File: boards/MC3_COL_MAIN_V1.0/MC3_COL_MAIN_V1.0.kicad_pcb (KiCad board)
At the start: 4 copper layers, 66 x 66 mm, 121 parts, among them J1 SUPPLY_IN, J10 MOTOR, J11 MOTOR, J12 CAN, J2 SWD, J3 ENC_leaf1, J4 ENC_leaf2, J5 ENC_leaf3, J6 ENC_leaf4, J7 MOTOR, J8 MOTOR, J9 MOTOR, Q1 AO4407C, SW1 SKRKAEE020, U1 AMS1117-3.3, U10 GP1S094HCZ0F, U11 GP1S094HCZ0F, U2 STM32F412RET6, U3 DRV8214RTER, U4 DRV8214RTER, U5 DRV8214RTER, U6 DRV8214RTER, U7 DRV8214RTER, U8 TJA1051T/3, U9 AEDR-8300-1Q0, Y1 8MHz

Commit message: WIP checkpoint before LED chain (board session state as on disk)
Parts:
- added C38: 1nF, MC3_COL_MAIN:C_0402_1005Metric, F.Cu at (85.8, 94.8)
- added C39: 1nF, MC3_COL_MAIN:C_0402_1005Metric, B.Cu at (81.0, 96.8)
- added C40: 1nF, MC3_COL_MAIN:C_0402_1005Metric, B.Cu at (76.0, 93.3)
- added C41: 1nF, MC3_COL_MAIN:C_0402_1005Metric, B.Cu at (79.2, 92.8)
- added C42: 1nF, MC3_COL_MAIN:C_0402_1005Metric, F.Cu at (86.2, 93.0)
- added C43: 100nF, MC3_COL_MAIN:C_0402_1005Metric, F.Cu at (108.0, 116.0)
- added H1: M2, MC3_COL_MAIN:MountingHole_2.2mm_M2, F.Cu at (89.5, 76.0)
- added H2: M2, MC3_COL_MAIN:MountingHole_2.2mm_M2, B.Cu at (125.5, 115.5)
- added H3: M2, MC3_COL_MAIN:MountingHole_2.2mm_M2, F.Cu at (100.0, 128.0)
- added H4: M2, MC3_COL_MAIN:MountingHole_2.2mm_M2, F.Cu at (125.0, 85.0)
- added H5: SLOT-PASSTHRU, MC3_COL_MAIN:SlotNPTH_PassThrough, F.Cu at (100.4, 73.8)
- U2: value STM32F412RET6 -> STM32U595RJT6
- moved J12 30.9 mm to (127.7, 102.0)
- moved R36 9.83 mm to (101.2, 117.0)
- moved U10 8.96 mm to (97.7, 119.1), turned to 83.23 degrees
- moved U11 8.57 mm to (102.3, 80.9), turned to 83.23 degrees
- moved TP7 8.06 mm to (129.8, 106.5)
- moved R37 7.17 mm to (100.8, 122.0)
- moved TP3 6.44 mm to (118.9, 114.0)
- moved C37 5.91 mm to (124.8, 107.0), turned to 180 degrees
- moved R33 2.57 mm to (120.3, 111.0), turned to 0 degrees
- moved TP2 2.35 mm to (127.2, 104.2)
- moved C6 2.12 mm to (84.2, 87.0), turned to 90 degrees
- moved C5 1.84 mm to (85.8, 97.8)
- moved TP1 1.68 mm to (115.1, 115.2)
- moved R35 1.57 mm to (122.2, 112.1)
- moved J11 0.64 mm to (97.5, 84.6)
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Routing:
- net /CAN/CANL: track 16.4 -> 49.7 mm
- net /CAN/CANH: track 27.8 -> 59.8 mm
- net /MCU/YAW_LIM: track 17.6 -> 34.4 mm, vias 0 -> 1
- net ENC_leaf2: track 38.3 -> 47.7 mm
- net +3V3: track 225.5 -> 231.6 mm
- net I2C1_SDA: track 94.6 -> 100.1 mm
- net I2C1_SCL: track 96.5 -> 102.0 mm
- net EN_leaf1: track 42.8 -> 47.4 mm
- net Net-(U11-A): track 4.84 -> 9.34 mm
- net /MCU/YAW_HOME: track 21.0 -> 24.7 mm, vias 0 -> 1
- net RC_OUT_leaf1: track 44.4 -> 48.0 mm
- net IPROPI_leaf3: track 47.3 -> 50.8 mm
- net PH_leaf1: track 42.8 -> 45.5 mm
- net IPROPI_leaf2: track 44.7 -> 47.4 mm
- net nFAULT_leaf1: track 38.4 -> 41.0 mm
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
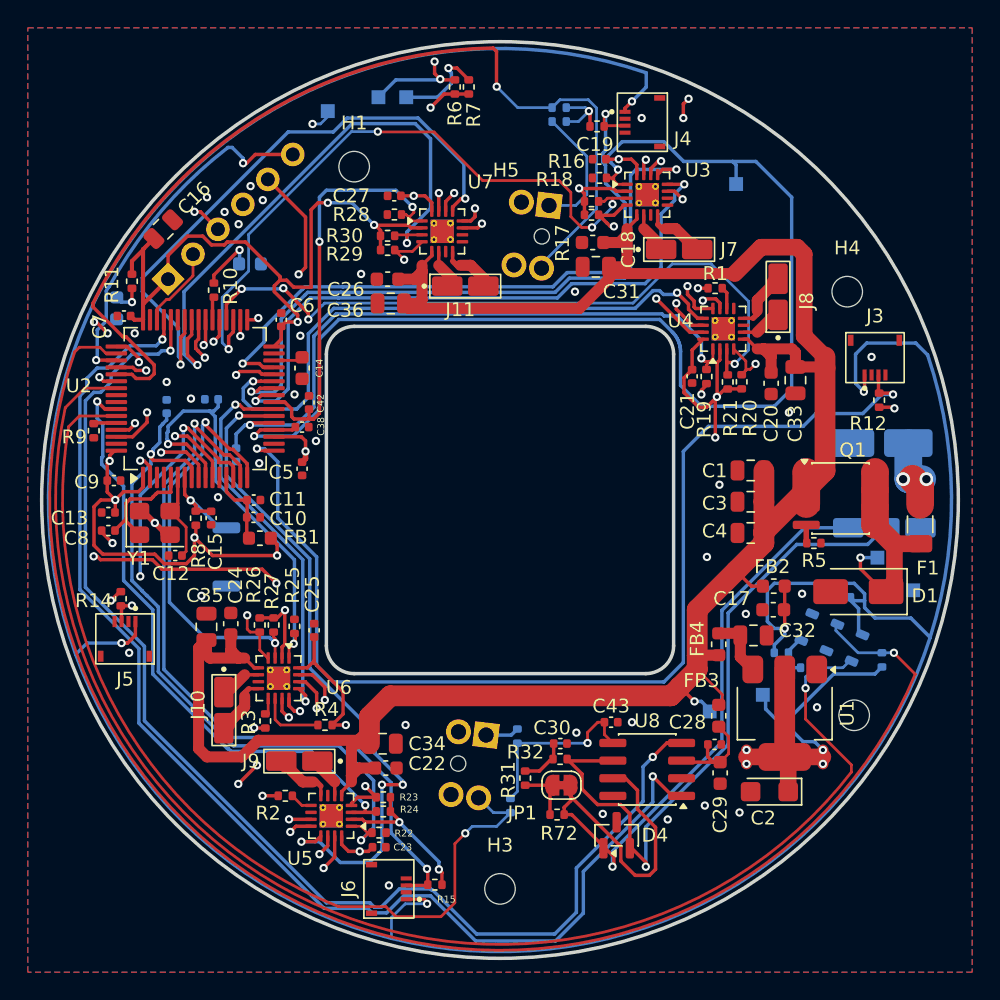
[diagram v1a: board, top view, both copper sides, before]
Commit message: V1.0: final 5 V-input state before the V1.1 fork (user board session: pixels placed, silk moves, FFC model update)
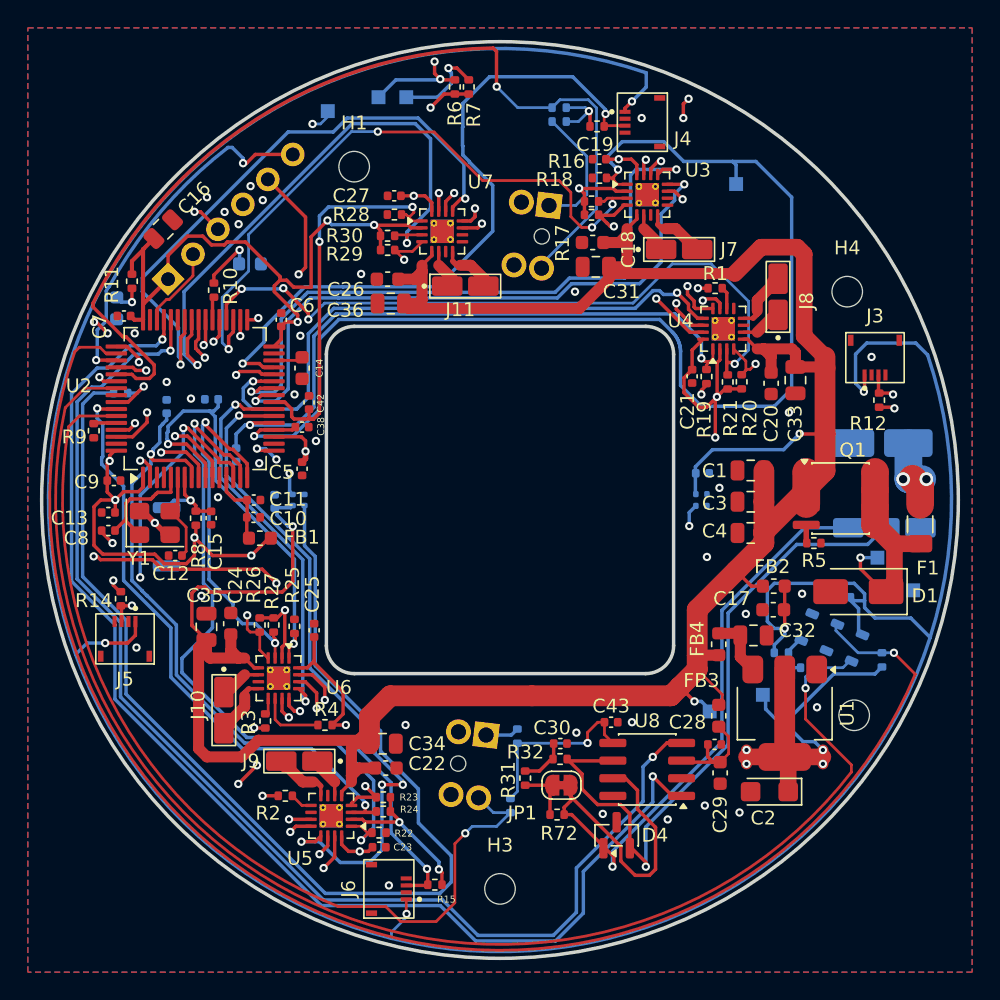
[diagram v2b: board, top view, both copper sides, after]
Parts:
- added C44: 100nF, MC3_COL_MAIN:C_0402_1005Metric, B.Cu at (83.8, 100.1)
- added C45: 100nF, MC3_COL_MAIN:C_0402_1005Metric, B.Cu at (114.6, 98.1)
- added D5: XL-1010RGBC-WS2812B, MC3_COL_MAIN:LED_XL-1010RGBC, B.Cu at (85.5, 100.0)
- added D6: XL-1010RGBC-WS2812B, MC3_COL_MAIN:LED_XL-1010RGBC, B.Cu at (114.5, 100.0)
- added R40: 470R, MC3_COL_MAIN:R_0402_1005Metric, B.Cu at (72.7, 92.3)
- H5: moved to B.Cu
- moved SW1 4.54 mm to (76.0, 102.7)
- moved H5 0.26 mm to (100.2, 73.8), turned to 180 degrees
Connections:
- U2 pad 57: unconnected-(U2-PB5-Pad57) -> /MCU/LED_DATA
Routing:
- net Net-(D5-DI): track 0.00 -> 85.9 mm
- net /MCU/LD1: track 0.00 -> 56.0 mm, vias 0 -> 2
- net VM: track 169.2 -> 200.8 mm, vias 1 -> 3
- net RC_OUT_leaf4: track 30.1 -> 26.0 mm
- net /MCU/LED_DATA: track 0.00 -> 3.79 mm, vias 0 -> 1
- net +3V3: track 231.6 -> 228.2 mm
- net VSENS: track 52.7 -> 49.8 mm
- net ENC_leaf2: track 47.7 -> 49.9 mm
- net IPROPI_yaw: track 30.6 -> 28.8 mm
- net /MCU/NRST: track 36.0 -> 34.6 mm
- net PH_leaf3: track 36.6 -> 37.9 mm
- net RC_OUT_leaf3: track 44.5 -> 43.3 mm
- net ENC_leaf4: track 53.9 -> 53.2 mm
- net IPROPI_leaf3: track 50.8 -> 50.1 mm
- net CAN1_TX: track 89.8 -> 89.3 mm
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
